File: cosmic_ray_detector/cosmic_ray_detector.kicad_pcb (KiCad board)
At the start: 4 copper layers, 80 x 60 mm, 56 parts, among them J1 MOLEX micro-fit 43045-0210, J2 5 pin pin header, J3 Black Banana, J4 Red Banana, J5 Green Banana, J6 BNC, U1 TL072, U2 TPS7A30, U3 TPS7A49, U4 TLV3501AIDBVTG4, U5 AD5270BRMZ-100-RL7

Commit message: routed
Signed-off-by: Dan Weatherill <daniel.weatherill@physics.ox.ac.uk>
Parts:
- moved J2 52.0 mm to (136.8, 76.2), turned to 0 degrees
- moved TP2 9.17 mm to (111.8, 103.5), turned to -90 degrees
- moved R9 5.75 mm to (117.9, 82.7), turned to -90 degrees
- moved C18 3.77 mm to (114.9, 87.5), turned to 90 degrees
- moved R10 3.45 mm to (116.2, 84.7), turned to -90 degrees
- moved U4 2.42 mm to (119.0, 86.0), turned to -90 degrees
- moved C17 2.12 mm to (116.2, 87.5), turned to 90 degrees
- moved C11 1.42 mm to (89.0, 103.3)
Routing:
- net GNDA: track 0.00 -> 48.1 mm, vias 0 -> 35
- net /comparator/V_IN: track 0.00 -> 34.2 mm
- net +5VA: track 0.00 -> 18.9 mm, vias 0 -> 11
- net /comparator/VREF: track 0.00 -> 18.3 mm, vias 0 -> 2
- net /detector_frontend/CSA_IN: track 0.00 -> 16.7 mm
- net /detector_frontend/CSA_FB: track 0.00 -> 12.6 mm
- net /comparator/COMP_OUT: track 0.00 -> 11.5 mm
- net Net-(C7-Pad2): track 0.00 -> 10.7 mm
- net /BIAS_IN: track 0.00 -> 10.2 mm
- net /threshold_setting/SPI.~{SYNC}: track 0.00 -> 7.92 mm
- net /threshold_setting/SPI.SCK: track 0.00 -> 7.60 mm
- net /Power Regulators/+VIN: track 0.00 -> 7.36 mm, vias 0 -> 2
- net /threshold_setting/SPI.SDI: track 0.00 -> 7.28 mm
- net -5VA: track 0.00 -> 7.12 mm, vias 0 -> 9
- net /threshold_setting/SPI.SDO: track 0.00 -> 6.97 mm
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- added copper zone on In1.Cu, net +5VA
- added copper zone on In2.Cu, net -5VA
- added copper zone on F.Cu, net /T_MID
- added copper zone on B.Cu, net GNDA

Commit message: silly diff pair tuning
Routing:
- net /threshold_setting/SPI.SDO: track 6.97 -> 7.95 mm
- net /threshold_setting/SPI.SDI: track 7.28 -> 7.92 mm
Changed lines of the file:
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@@
   (segment (start 109.325 75.798929) (end 109.325 81) (width 0.25) (layer "F.Cu") (net 18))
   (arc (start 109.500736 75.374665) (mid 109.370672 75.569319) (end 109.325 75.798929) (width 0.25) (layer "F.Cu") (net 18))
-  (segment (start 133.25 79) (end 136.02 76.23) (width 0.2) (layer "F.Cu") (net 19))
   (segment (start 136.02 76.23) (end 136.75 76.23) (width 0.2) (layer "F.Cu") (net 19))
   (segment (start 129.975 79) (end 133.25 79) (width 0.2) (layer "F.Cu") (net 19))
-  (segment (start 134.105335 79.5) (end 136.105335 77.5) (width 0.2) (layer "F.Cu") (net 20))
-  (segment (start 136.105335 77.5) (end 136.75 77.5) (width 0.2) (layer "F.Cu") (net 20))
-  (segment (start 129.975 79.5) (end 134.105335 79.5) (width 0.2) (layer "F.Cu") (net 20))
-  (segment (start 135.52 80) (end 136.75 78.77) (width 0.2) (layer "F.Cu") (net 21))
-  (segment (start 129.975 80) (end 135.52 80) (width 0.2) (layer "F.Cu") (net 21))
-  (segment (start 136.29 80.5) (end 136.75 80.04) (width 0.2) (layer "F.Cu") (net 22))
-  (segment (start 129.975 80.5) (end 136.29 80.5) (width 0.2) (layer "F.Cu") (net 22))
+  (segment (start 133.25 79) (end 136.02 76.23) (width 0.2) (layer "F.Cu") (net 19))
+  (segment (start 134.821292 78.784041) (end 134.704139 78.901195) (width 0.2) (layer "F.Cu") (net 20))
+  (segment (start 134.704139 78.901195) (end 134.105335 79.5) (width 0.2) (layer "F.Cu") (net 20))
+  (segment (start 134.938446 78.052666) (end 134.938446 78.052667) (width 0.2) (layer "F.Cu") (net 20))
+  (segment (start 136.105335 77.5) (end 135.552668 78.052667) (width 0.2) (layer "F.Cu") (net 20))
+  (segment (start 136.75 77.5) (end 136.105335 77.5) (width 0.2) (layer "F.Cu") (net 20))
+  (segment (start 134.821291 78.784042) (end 134.821292 78.784041) (width 0.2) (layer "F.Cu") (net 20))
+  (segment (start 134.938446 78.052667) (end 134.821292 78.16982) (width 0.2) (layer "F.Cu") (net 20))
+  (segment (start 134.105335 79.5) (end 129.975 79.5) (width 0.2) (layer "F.Cu") (net 20))
+  (segment (start 134.821292 78.47693) (end 134.821292 78.476931) (width 0.2) (layer "F.Cu") (net 20))
+  (segment (start 135.245556 78.052667) (end 135.245557 78.052667) (width 0.2) (layer "F.Cu") (net 20))
+  (arc (start 135.552668 78.052667) (mid 135.399112 78.116272) (end 135.245556 78.052667) (width 0.2) (layer "F.Cu") (net 20))
+  (arc (start 134.821292 78.16982) (mid 134.757687 78.323375) (end 134.821292 78.47693) (width 0.2) (layer "F.Cu") (net 20))
+  (arc (start 134.821292 78.476931) (mid 134.884896 78.630487) (end 134.821291 78.784042) (width 0.2) (layer "F.Cu") (net 20))
+  (arc (start 135.245557 78.052667) (mid 135.092002 77.989062) (end 134.938446 78.052666) (width 0.2) (layer "F.Cu") (net 20))
+  (segment (start 136.75 78.77) (end 135.52 80) (width 0.2) (layer "F.Cu") (net 21))
+  (segment (start 132.78275 80) (end 129.975 80) (width 0.2) (layer "F.Cu") (net 21))
+  (segment (start 134.32 80) (end 132.78275 80) (width 0.2) (layer "F.Cu") (net 21))
+  (arc (start 135.52 80) (mid 135.307868 79.912132) (end 135.22 79.7) (width 0.2) (layer "F.Cu") (net 21))
+  (arc (start 134.92 79.4) (mid 134.707868 79.487868) (end 134.62 79.7) (width 0.2) (layer "F.Cu") (net 21))
+  (arc (start 134.62 79.7) (mid 134.532132 79.912132) (end 134.32 80) (width 0.2) (layer "F.Cu") (net 21))
+  (arc (start 135.22 79.7) (mid 135.132132 79.487868) (end 134.92 79.4) (width 0.2) (layer "F.Cu") (net 21))
+  (segment (start 136.75 80.04) (end 136.29 80.5) (width 0.2) (layer "F.Cu") (net 22))
+  (segment (start 133.3 80.5) (end 132.110419 80.5) (width 0.2) (layer "F.Cu") (net 22))
+  (segment (start 134.2 80.8) (end 134.2 80.974756) (width 0.2) (layer "F.Cu") (net 22))
+  (segment (start 132.110419 80.5) (end 129.975 80.5) (width 0.2) (layer "F.Cu") (net 22))
+  (segment (start 136.29 80.5) (end 134.5 80.5) (width 0.2) (layer "F.Cu") (net 22))
+  (segment (start 133.6 80.974756) (end 133.6 80.8) (width 0.2) (layer "F.Cu") (net 22))
+  (arc (start 134.2 80.974756) (mid 134.112132 81.186888) (end 133.9 81.274756) (width 0.2) (layer "F.Cu") (net 22))
+  (arc (start 133.9 81.274756) (mid 133.687868 81.186888) (end 133.6 80.974756) (width 0.2) (layer "F.Cu") (net 22))
+  (arc (start 133.6 80.8) (mid 133.512132 80.587868) (end 133.3 80.5) (width 0.2) (layer "F.Cu") (net 22))
+  (arc (start 134.5 80.5) (mid 134.287868 80.587868) (end 134.2 80.8) (width 0.2) (layer "F.Cu") (net 22))
   (segment (start 124.8819 92.3781) (end 127.691 92.3781) (width 0.2) (layer "F.Cu") (net 23))
   (segment (start 124.76 92.5) (end 124.8819 92.3781) (width 0.2) (layer "F.Cu") (net 23))

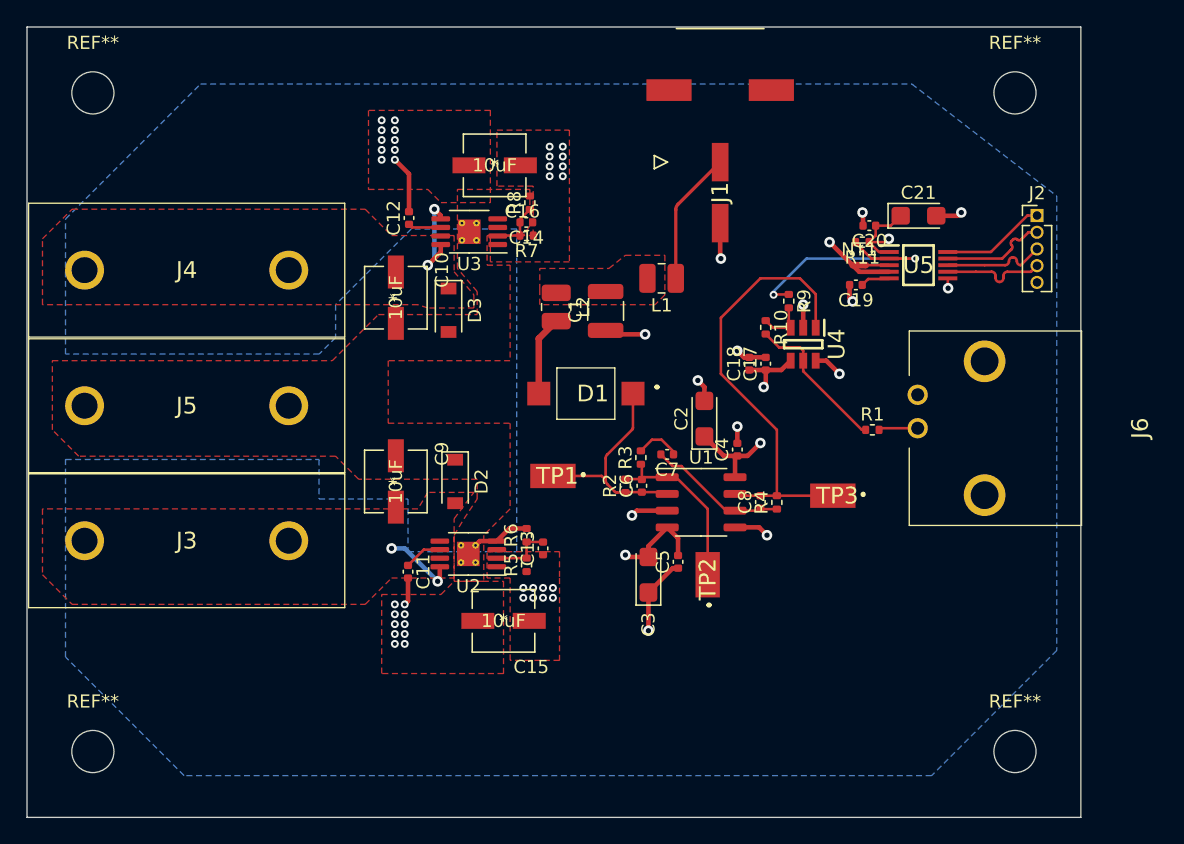
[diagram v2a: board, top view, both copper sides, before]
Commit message: footprint fix, clear all DRC errors, now just warnings
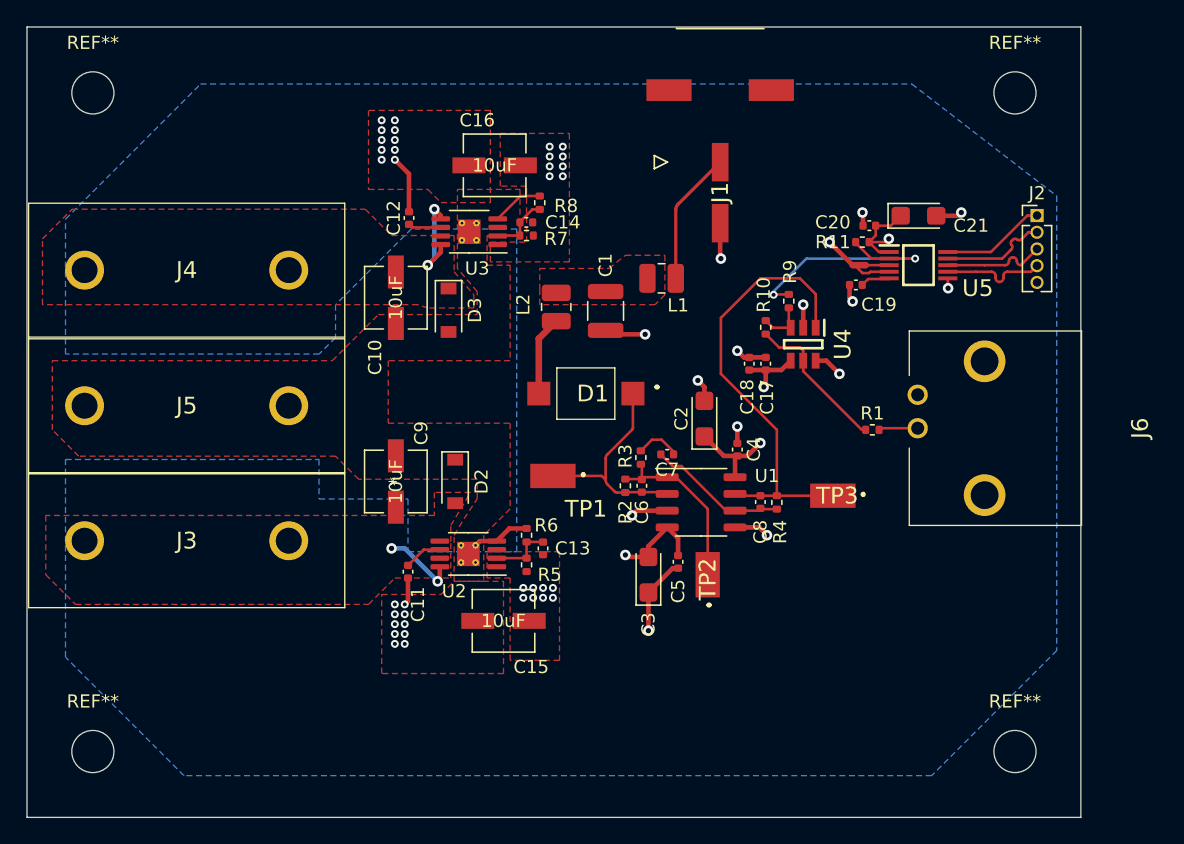
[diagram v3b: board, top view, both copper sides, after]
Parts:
- moved R8 0.75 mm to (99.0, 75.3)
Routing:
- net GNDA: track 48.1 -> 51.9 mm
- net Net-(C14-Pad2): track 3.99 -> 4.63 mm

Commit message: all DRC passes no warnings
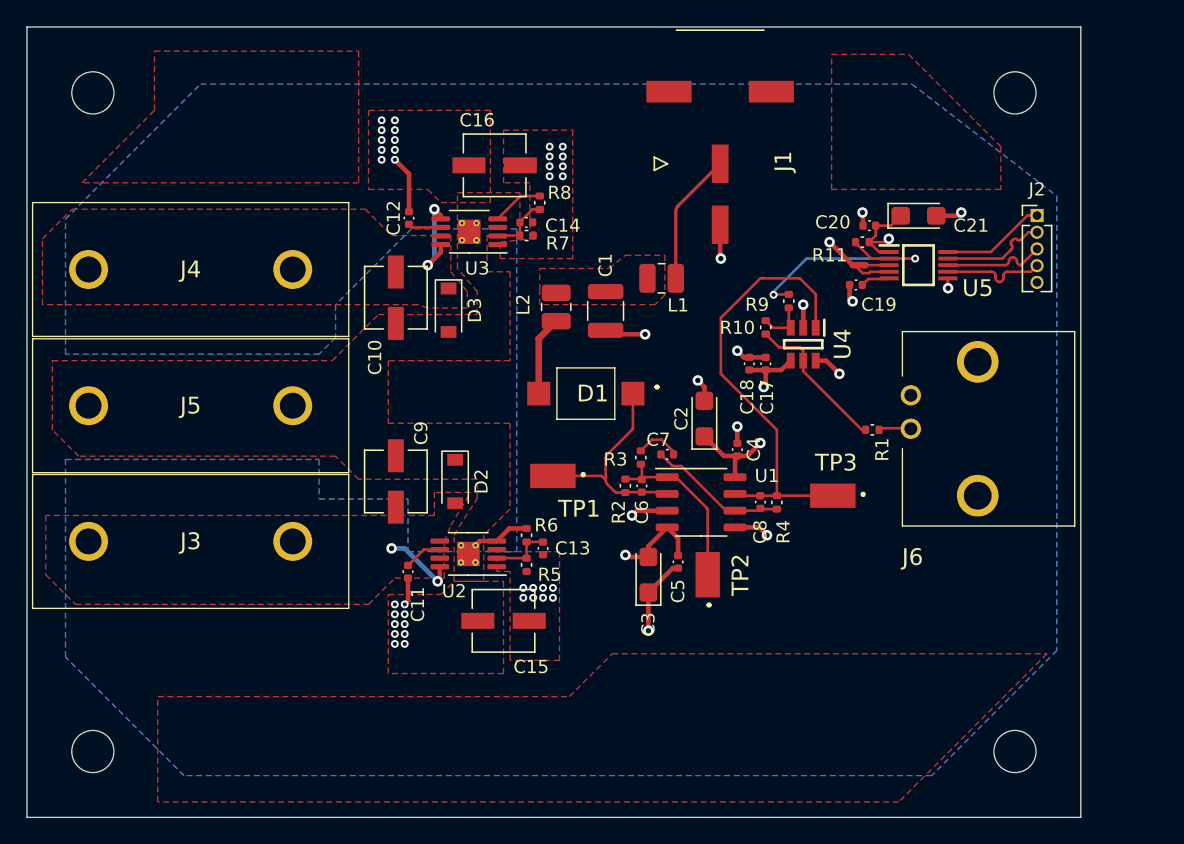
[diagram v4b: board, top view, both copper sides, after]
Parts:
- C11, C12, C13, C14, C17, C18, C19, C20, C4, C5, C6, C7, C8: footprint Capacitor_SMD:C_0402_1005Metric -> cosmic_ray_detector_lib:C_0402_1005Metric
- D2, D3: footprint Diode_SMD:D_SOD-123 -> cosmic_ray_detector_lib:D_SOD-123
- R1, R10, R11, R2, R3, R4, R5, R6, R7, R8, R9: footprint Resistor_SMD:R_0402_1005Metric -> cosmic_ray_detector_lib:R_0402_1005Metric
- moved J6 0.52 mm to (127.2, 92.4)
- moved J3 0.31 mm to (64.8, 101.0)
- moved J4 0.31 mm to (64.8, 80.3)
- moved J5 0.30 mm to (64.8, 90.7)
- moved J1 0.12 mm to (112.7, 74.6)
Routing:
- added copper zone on F.Cu, net (none)
- added copper zone on In1.Cu, net (none)
- added copper zone on In2.Cu, net (none)
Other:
- rule pad_to_mask_clearance: 0 -> 0.125

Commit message: include local copies of modified footprints (for DRC) add some nice labels
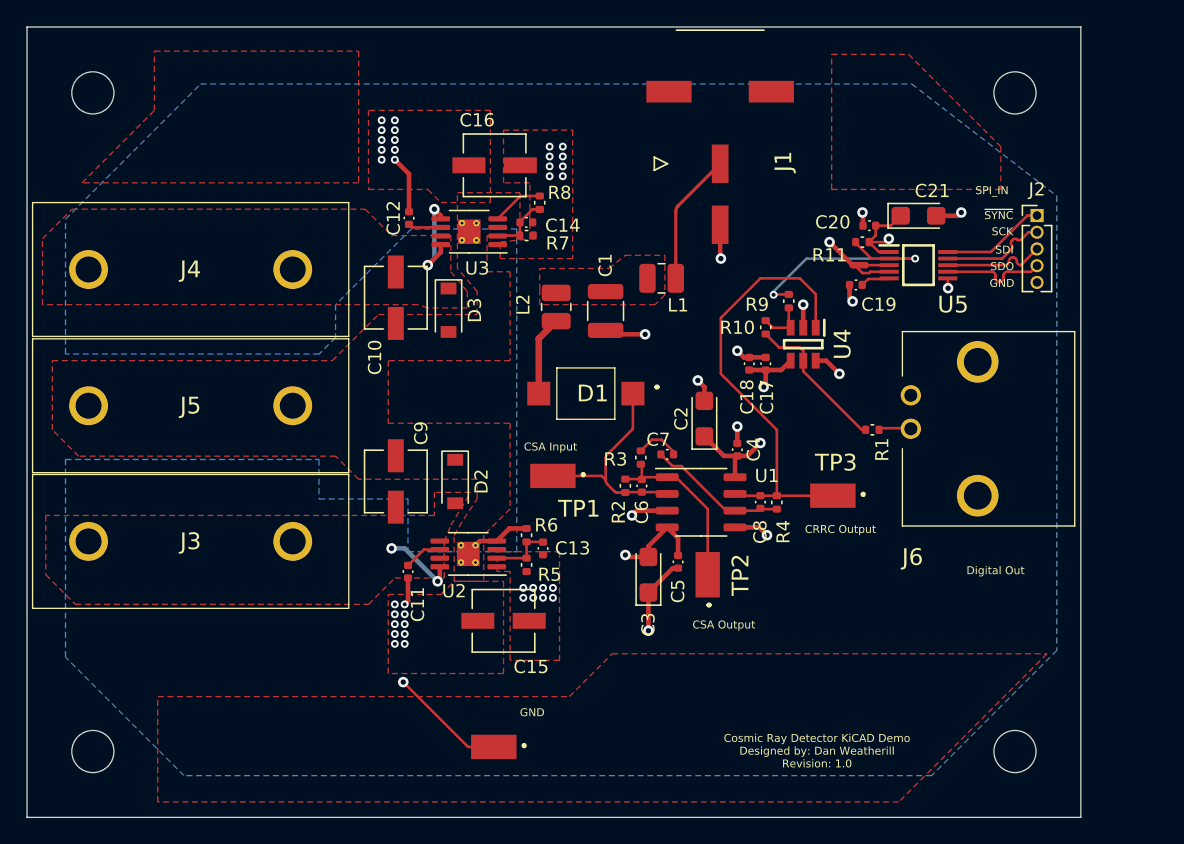
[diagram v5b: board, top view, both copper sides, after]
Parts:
- added TP4: ~, cosmic_ray_detector_lib:harwin_tp_SMD, F.Cu at (95.5, 116.6)
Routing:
- net GNDA: track 51.9 -> 60.8 mm, vias 35 -> 36
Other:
- board text added: "CRRC Output"
- board text added: "CSA Input"
- board text added: "CSA Output"
- board text added: "Cosmic Ray Detector KiCAD Demo Designed by: Dan Weatherill Revision: 1.0"
- board text added: "Digital Out"
- board text added: "GND"
- board text added: "SCK"
- board text added: "SDI"
- board text added: "SDO"
- board text added: "SPI_IN"
- board text added: "~{SYNC}"
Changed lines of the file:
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@@
   )
   (paper "A4")
+  (title_block
+    (title "Cosmic Ray Detector")
+    (date "2022-05-26")
+    (rev "1")
+    (company "AITL")
+    (comment 1 "Design by: Dan Weatherill")
+  )
   (layers
     (0 "F.Cu" signal)
@@
   )
   (footprint "cosmic_ray_detector_lib:harwin_tp_SMD" (layer "F.Cu")
+    (at 95.5125 116.57)
+    (descr "S1751-46R-1")
+    (tags "Test Point")
+    (property "Farnell" "2293786")
+    (property "MPN" "S1751-46R")
+    (property "Manufacturer_Name" "Harwin")
+    (property "Sheetfile" "frontend.kicad_sch")
+    (property "Sheetname" "detector_frontend")
+    (attr smd board_only)
+    (fp_text reference "TP4" (at 0 -2.5) (layer "F.SilkS") hide
+      (effects (font (size 1.27 1.27) (thickness 0.254)))
+    )
+    (fp_text value "~" (at 0.337 0) (layer "F.SilkS") hide
+      (effects (font (size 1.27 1.27) (thickness 0.254)))
+    )
+    (fp_text user "${REFERENCE}" (at 0 -2.75) (layer "F.Fab")
+      (effects (font (size 1.27 1.27) (thickness 0.254)))
+    )
+    (fp_line (start 2.3 -0.2) (end 2.3 -0.2) (layer "F.SilkS") (width 0.2))
+    (fp_line (start 2.3 0) (end 2.3 0) (layer "F.SilkS") (width 0.2))
+    (fp_arc (start 2.3 0) (mid 2.2 -0.1) (end 2.3 -0.2) (layer "F.SilkS") (width 0.2))
+    (fp_arc (start 2.3 -0.2) (mid 2.4 -0.1) (end 2.3 0) (layer "F.SilkS") (width 0.2))
+    (fp_line (start -2.225 -1.425) (end 2.9 -1.425) (layer "F.CrtYd") (width 0.1))
+    (fp_line (start 2.9 -1.425) (end 2.9 1.425) (layer "F.CrtYd") (width 0.1))
+    (fp_line (start -2.225 1.425) (end -2.225 -1.425) (layer "F.CrtYd") (width 0.1))
+    (fp_line (start 2.9 1.425) (end -2.225 1.425) (layer "F.CrtYd") (width 0.1))
+    (fp_line (start 1.625 0.825) (end -1.625 0.825) (layer "F.Fab") (width 0.2))
+    (fp_line (start -1.625 -0.825) (end 1.625 -0.825) (layer "F.Fab") (width 0.2))
+    (fp_line (start 1.625 -0.825) (end 1.625 0.825) (layer "F.Fab") (width 0.2))
+    (fp_line (start -1.625 0.825) (end -1.625 -0.825) (layer "F.Fab") (width 0.2))
+    (pad "1" smd rect (at 0 0 90) (size 1.85 3.45) (layers "F.Cu" "F.Paste" "F.Mask")
+      (net 30 "GNDA") (pinfunction "1") (pintype "passive"))
+    (model "${KIPRJMOD}/../parts/harwin_testpoints/s1751-46r.stp"
+      (offset (xyz 0 0.85 2))
+      (scale (xyz 1 1 1))
+      (rotate (xyz -90 0 0))
+    )
+  )
+  (footprint "cosmic_ray_detector_lib:harwin_tp_SMD" (layer "F.Cu")
     (at 100 96)
     (descr "S1751-46R-1")
@@
     (clearance 0.2)
     (attr smd)
-    (fp_text reference "U5" (at 4.5 1.75) (layer "F.SilkS")
+    (fp_text reference "U5" (at 2.63 3) (layer "F.SilkS")
       (effects (font (size 1.27 1.27) (thickness 0.254)))
     )
@@
     (property "Sheetname" "threshold_setting")
     (attr smd)
-    (fp_text reference "C21" (at 4 0.75) (layer "F.SilkS")
+    (fp_text reference "C21" (at 1.06 -1.88) (layer "F.SilkS")
       (effects (font (size 1 1) (thickness 0.15)))
     )
@@
   (gr_line (start 91.696901 68.1281) (end 93.446901 74.6281) (layer "Cmts.User") (width 0.15))
   (gr_rect (start 60.076 61.92) (end 140.076 121.92) (layer "Edge.Cuts") (width 0.1) (fill none))
+  (gr_text "~{SYNC}" (at 133.85 76.22) (layer "F.SilkS")
+    (effects (font (size 0.6 0.6) (thickness 0.1)))
+  )
+  (gr_text "SDI" (at 134.278571 78.84) (layer "F.SilkS")
+    (effects (font (size 0.6 0.6) (thickness 0.1)))
+  )
+  (gr_text "SDO" (at 134.107143 80.1) (layer "F.SilkS")
+    (effects (font (size 0.6 0.6) (thickness 0.1)))
+  )
+  (gr_text "Digital Out" (at 133.6 103.18) (layer "F.SilkS")
+    (effects (font (size 0.6 0.6) (thickness 0.1)))
+  )
+  (gr_text "Cosmic Ray Detector KiCAD Demo\nDesigned by: Dan Weatherill\nRevision: 1.0\n" (at 120.05 116.88) (layer "F.SilkS")
+    (effects (font (size 0.6 0.6) (thickness 0.1)))
+  )
+  (gr_text "SPI_IN" (at 133.33 74.33) (layer "F.SilkS")
+    (effects (font (size 0.6 0.6) (thickness 0.1)))
+  )
+  (gr_text "GND" (at 134.092857 81.37) (layer "F.SilkS")
+    (effects (font (size 0.6 0.6) (thickness 0.1)))
+  )
+  (gr_text "GND" (at 98.43 113.96) (layer "F.SilkS")
+    (effects (font (size 0.6 0.6) (thickness 0.1)))
+  )
+  (gr_text "SCK" (at 134.121428 77.45) (layer "F.SilkS")
+    (effects (font (size 0.6 0.6) (thickness 0.1)))
+  )
+  (gr_text "CRRC Output" (at 121.83 100.05) (layer "F.SilkS")
+    (effects (font (size 0.6 0.6) (thickness 0.1)))
+  )
+  (gr_text "CSA Input" (at 99.82 93.79) (layer "F.SilkS")
+    (effects (font (size 0.6 0.6) (thickness 0.1)))
+  )
+  (gr_text "CSA Output" (at 112.98 107.3) (layer "F.SilkS")
+    (effects (font (size 0.6 0.6) (thickness 0.1)))
+  )
   (gr_text "NOTE: Always follow datasheet recommendations\non layout, especially for regulators & the like.\n\nHere, note that the pin {dblquote}5{dblquote} is just the {dblquote}enable{dblquote} pin,\nwe really want all the current through VIN net to go to\npin 8" (at 91.696901 62.8781) (layer "Cmts.User")
     (effects (font (size 1 1) (thickness 0.15)))
@@
   (segment (start 123.998327 80.599511) (end 123.501673 80.599511) (width 0.2) (layer "F.Cu") (net 30))
   (segment (start 89.076 75.94) (end 89.076 73.076) (width 0.35) (layer "F.Cu") (net 30))
+  (segment (start 95.5125 116.57) (end 93.56 116.57) (width 0.2) (layer "F.Cu") (net 30))
   (segment (start 124.097838 80.5) (end 123.998327 80.599511) (width 0.2) (layer "F.Cu") (net 30))
   (segment (start 95.7385 100.945) (end 94.451 100.945) (width 0.35) (layer "F.Cu") (net 30))
@@
   (segment (start 123 80.097838) (end 123 80) (width 0.2) (layer "F.Cu") (net 30))
   (segment (start 119 84.75) (end 119 83) (width 0.35) (layer "F.Cu") (net 30))
+  (segment (start 93.56 116.57) (end 88.64 111.65) (width 0.2) (layer "F.Cu") (net 30))
   (segment (start 99 74.75) (end 97.5435 74.75) (width 0.2) (layer "F.Cu") (net 30))
   (segment (start 123.54 76.04) (end 123.5 76) (width 0.35) (layer "F.Cu") (net 30))
@@
   (segment (start 123.501673 80.599511) (end 123 80.097838) (width 0.2) (layer "F.Cu") (net 30))
   (segment (start 113.825 99.905) (end 115.655 99.905) (width 0.35) (layer "F.Cu") (net 30))
+  (via (at 88.64 111.65) (size 0.8) (drill 0.4) (layers "F.Cu" "B.Cu") (net 30))
   (via (at 88.75 108) (size 0.6) (drill 0.3) (layers "F.Cu" "B.Cu") (free) (net 30))
   (via (at 87 70.5) (size 0.6) (drill 0.3) (layers "F.Cu" "B.Cu") (free) (net 30))
